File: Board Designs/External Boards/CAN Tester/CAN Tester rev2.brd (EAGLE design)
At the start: 83.8 x 100.3 mm, 27 parts, among them M1 Minifit, M2 Nanofit, M3 Nanofit-1, M4 Minifit-1, U1 ISOLATED CAN TRANSCIEVER, U3 TEENSY_3.2_SIMPLE, U4 CHARACTER_LCD

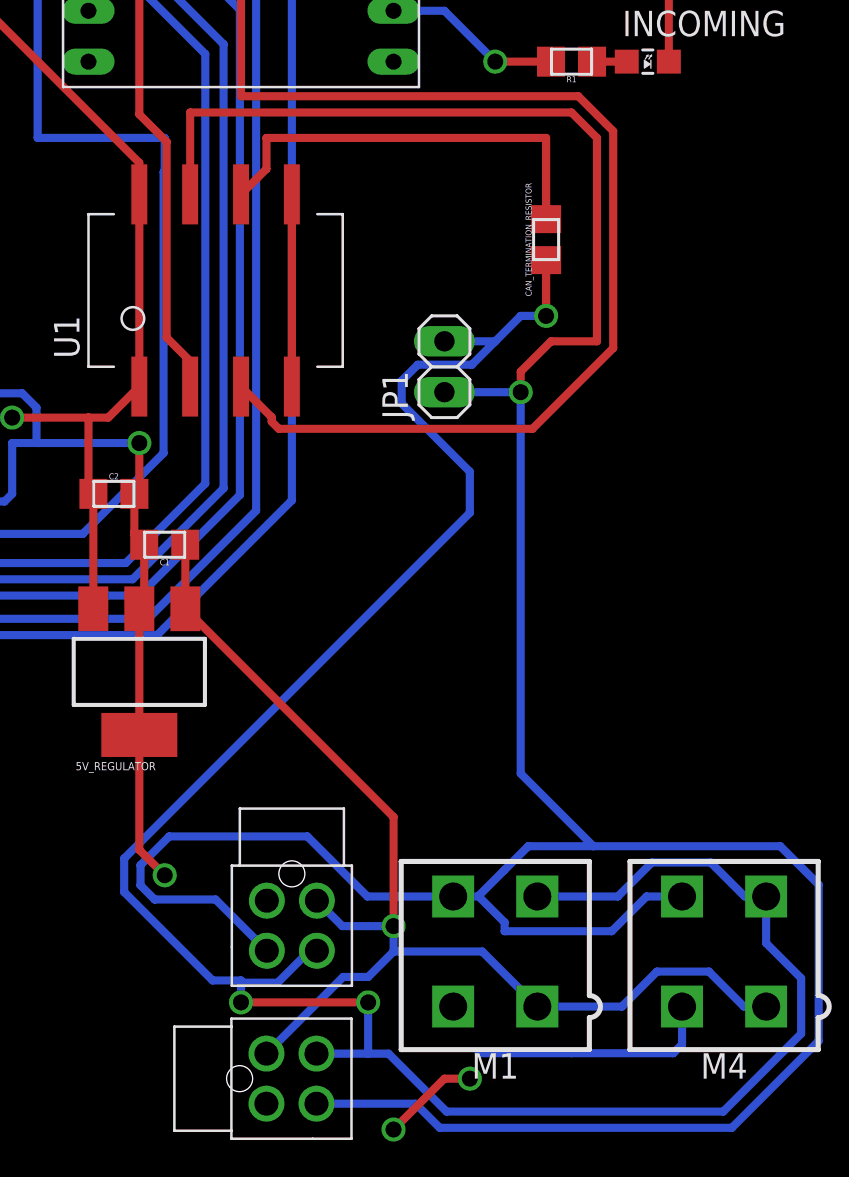
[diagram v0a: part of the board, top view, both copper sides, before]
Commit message: Began work on Rev 2 of CAN_Tester, fixing the existing issues with the Rev 1 board but not isolating the isocan yet.
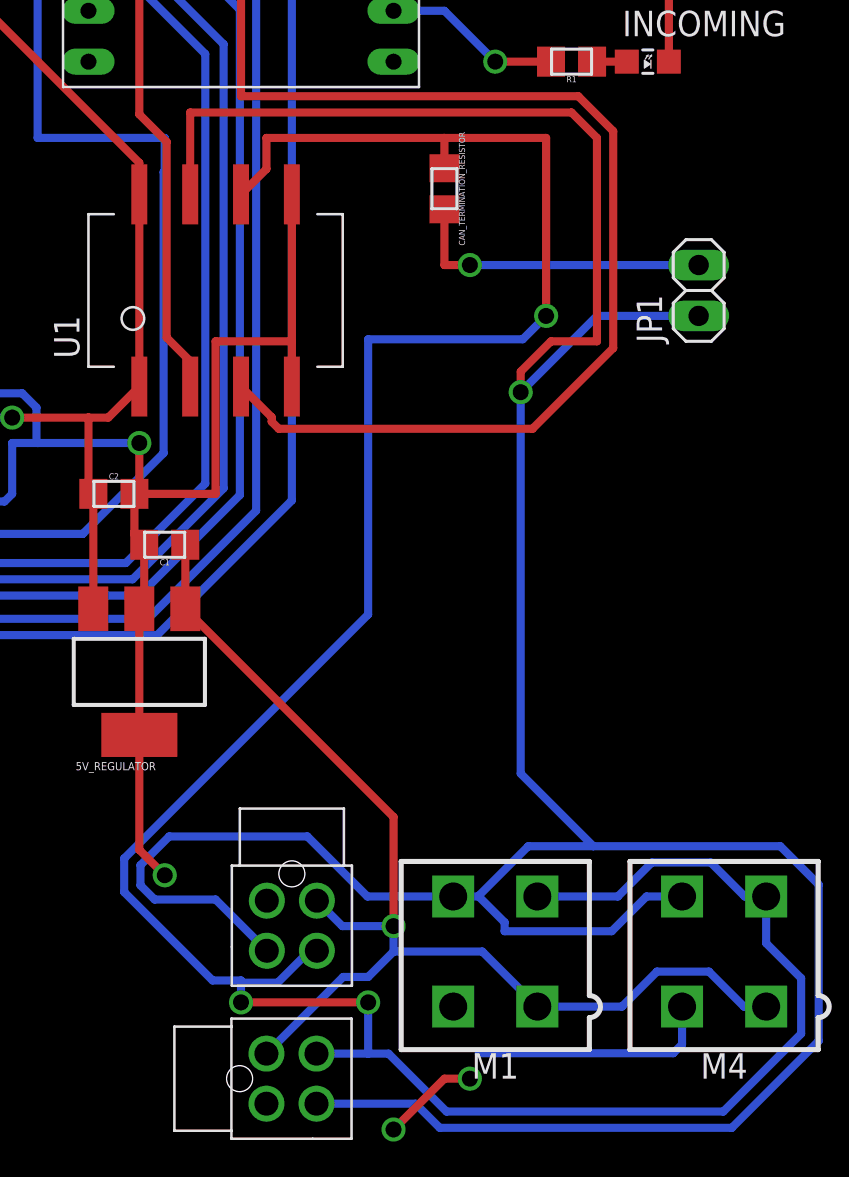
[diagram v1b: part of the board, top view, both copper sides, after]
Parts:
- moved JP1 13.3 mm to (74.9, 47.0)
- moved CAN_TERMINATION_RESISTOR 5.68 mm to (62.2, 52.1), turned to 270 degrees
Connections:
- removed net N$16: U1.P$4, U1.P$5
- new net N$15: CAN_TERMINATION_RESISTOR.2, JP1.2
- net CANL: no longer CAN_TERMINATION_RESISTOR.2, JP1.2
- net GND: now also U1.P$4, U1.P$5
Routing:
- net GND: track 213.6 -> 238.7 mm
- net N$15: track 0.00 -> 15.5 mm, vias 0 -> 1
- net N$16: track 9.60 -> 0.00 mm
- net CANH: track 161.8 -> 168.5 mm
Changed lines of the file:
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@@
 <?xml version="1.0" encoding="utf-8"?>
 <!DOCTYPE eagle SYSTEM "eagle.dtd">
-<eagle version="9.2.1">
+<eagle version="9.2.2">
 <drawing>
 <settings>
@@
 <attribute name="VALUE" x="45.72" y="36.1188" size="0.3048" layer="27" align="top-center"/>
 </element>
-<element name="CAN_TERMINATION_RESISTOR" library="HyTechDevices" package="0805" value="120" x="67.31" y="49.53" smashed="yes" rot="R90">
-<attribute name="NAME" x="66.5861" y="49.53" size="0.3048" layer="25" rot="R90" align="bottom-center"/>
-<attribute name="VALUE" x="68.0212" y="49.53" size="0.3048" layer="27" rot="R90" align="top-center"/>
+<element name="CAN_TERMINATION_RESISTOR" library="HyTechDevices" package="0805" value="120" x="62.23" y="52.07" smashed="yes" rot="R270">
+<attribute name="NAME" x="62.9539" y="52.07" size="0.3048" layer="25" rot="R270" align="bottom-center"/>
+<attribute name="VALUE" x="61.5188" y="52.07" size="0.3048" layer="27" rot="R270" align="top-center"/>
 </element>
 <element name="CONTRAST_POT" library="HyTechDevices" package="TRIM-3386" value="10k" x="33.02" y="88.9" smashed="yes" rot="R180">
@@
 <attribute name="VALUE" x="76.2" y="20.32" size="1.27" layer="27" align="bottom-center"/>
 </element>
-<element name="JP1" library="HyTechDevices" package="1X02" value="M02" x="62.23" y="43.18" smashed="yes" rot="R90">
-<attribute name="NAME" x="60.4012" y="40.5638" size="1.27" layer="25" ratio="10" rot="R90"/>
-<attribute name="VALUE" x="65.405" y="40.64" size="1.27" layer="27" rot="R90"/>
+<element name="JP1" library="HyTechDevices" package="1X02" value="M02" x="74.93" y="46.99" smashed="yes" rot="R90">
+<attribute name="NAME" x="73.1012" y="44.3738" size="1.27" layer="25" ratio="10" rot="R90"/>
+<attribute name="VALUE" x="78.105" y="44.45" size="1.27" layer="27" rot="R90"/>
 </element>
 </elements>
@@
 <contactref element="M1" pad="3"/>
 <contactref element="U1" pad="P$6"/>
-<contactref element="CAN_TERMINATION_RESISTOR" pad="1"/>
-<contactref element="CAN_TERMINATION_RESISTOR" pad="2"/>
 <contactref element="M3" pad="P$3"/>
 <contactref element="M4" pad="3"/>
 <wire x1="52.07" y1="51.79" x2="53.34" y2="53.06" width="0.4064" layer="1"/>
 <wire x1="53.34" y1="53.06" x2="53.34" y2="54.61" width="0.4064" layer="1"/>
-<wire x1="53.34" y1="54.61" x2="67.31" y2="54.61" width="0.4064" layer="1"/>
-<wire x1="67.31" y1="54.61" x2="67.31" y2="50.555" width="0.4064" layer="1"/>
 <wire x1="72.59211875" y1="18.4177" x2="75.53168125" y2="18.4177" width="0.4064" layer="16"/>
 <wire x1="66.87" y1="16.72" x2="70.89441875" y2="16.72" width="0.4064" layer="16"/>
@@
 <wire x1="80.0485" y1="12.63898125" x2="78.3" y2="14.38748125" width="0.4064" layer="16"/>
 <wire x1="78.3" y1="14.38748125" x2="78.3" y2="16.72" width="0.4064" layer="16"/>
-<wire x1="46.2344" y1="16.9409625" x2="46.2344" y2="18.6190375" width="0.4064" layer="16"/>
-<wire x1="63.5" y1="35.8846375" x2="46.2344" y2="18.6190375" width="0.4064" layer="16"/>
+<wire x1="46.2344" y1="18.6190375" x2="46.2344" y2="16.9409625" width="0.4064" layer="16"/>
 <wire x1="53.89858125" y1="12.4115" x2="52.07" y2="12.4115" width="0.4064" layer="16"/>
 <wire x1="52.07" y1="12.5258" x2="50.6495625" y2="12.5258" width="0.4064" layer="16"/>
@@
 <wire x1="58.42" y1="11.43" x2="58.42" y2="8.87" width="0.4064" layer="16"/>
 <wire x1="52.07" y1="12.4115" x2="52.07" y2="11.43" width="0.4064" layer="16"/>
-<contactref element="JP1" pad="2"/>
-<wire x1="67.31" y1="48.505" x2="67.31" y2="45.72" width="0.4064" layer="1"/>
 <via x="67.31" y="45.72" extent="1-16" drill="0.8" diameter="0.8"/>
-<wire x1="64.77" y1="44.45" x2="62.23" y2="44.45" width="0.4064" layer="16"/>
-<wire x1="67.31" y1="45.72" x2="66.04" y2="45.72" width="0.4064" layer="16"/>
-<wire x1="66.04" y1="45.72" x2="64.77" y2="44.45" width="0.4064" layer="16"/>
-<wire x1="60.8998625" y1="43.2816" x2="60.0964" y2="42.4781375" width="0.4064" layer="16"/>
-<wire x1="60.0964" y1="42.4781375" x2="60.0964" y2="41.3418625" width="0.4064" layer="16"/>
-<wire x1="60.0964" y1="41.3418625" x2="63.5" y2="37.9382625" width="0.4064" layer="16"/>
-<wire x1="63.5" y1="37.9382625" x2="63.5" y2="35.8846375" width="0.4064" layer="16"/>
-<wire x1="64.77" y1="44.45" x2="63.6016" y2="43.2816" width="0.4064" layer="16"/>
-<wire x1="63.6016" y1="43.2816" x2="60.8998625" y2="43.2816" width="0.4064" layer="16"/>
-<wire x1="67.31" y1="48.505" x2="67.31" y2="50.555" width="0" layer="19" extent="1-1"/>
+<wire x1="67.31" y1="54.61" x2="67.31" y2="45.72" width="0.4064" layer="1"/>
+<wire x1="53.34" y1="54.61" x2="62.23" y2="54.61" width="0.4064" layer="1"/>
+<wire x1="62.23" y1="54.61" x2="67.31" y2="54.61" width="0.4064" layer="1"/>
+<wire x1="67.31" y1="45.72" x2="66.1416" y2="44.5516" width="0.4064" layer="16"/>
+<wire x1="66.1416" y1="44.5516" x2="58.42" y2="44.5516" width="0.4064" layer="16"/>
+<wire x1="58.42" y1="44.5516" x2="58.42" y2="30.8046375" width="0.4064" layer="16"/>
+<wire x1="58.42" y1="30.8046375" x2="46.2344" y2="18.6190375" width="0.4064" layer="16"/>
+<contactref element="CAN_TERMINATION_RESISTOR" pad="1"/>
+<wire x1="62.23" y1="53.095" x2="62.23" y2="54.61" width="0.4064" layer="1"/>
 </signal>
 <signal name="GND">
@@
 <wire x1="66.80318125" y1="84.3534" x2="67.8266" y2="84.3534" width="0.4064" layer="1"/>
 <wire x1="67.8266" y1="84.3534" x2="73.44" y2="78.74" width="0.4064" layer="1"/>
-<wire x1="46.99" y1="24.79" x2="46.99" y2="24.13" width="0.4064" layer="1"/>
-<wire x1="46.99" y1="24.13" x2="46.99" y2="19.05" width="0.4064" layer="1"/>
+<wire x1="46.99" y1="24.79" x2="46.99" y2="19.05" width="0.4064" layer="1"/>
 <wire x1="46.99" y1="19.05" x2="48.26" y2="17.78" width="0.4064" layer="1"/>
 <via x="48.26" y="17.78" extent="1-16" drill="0.8" diameter="0.8"/>
-<wire x1="63.94" y1="8.89" x2="68.58" y2="8.89" width="0.4064" layer="16"/>
-<wire x1="68.58" y1="8.89" x2="73.66" y2="8.89" width="0.4064" layer="16"/>
+<wire x1="63.94" y1="8.89" x2="73.66" y2="8.89" width="0.4064" layer="16"/>
 <wire x1="73.66" y1="8.89" x2="74.1" y2="9.33" width="0.4064" layer="16"/>
 <wire x1="74.1" y1="9.33" x2="74.1" y2="11.22" width="0.4064" layer="16"/>
@@
 <wire x1="62.23" y1="7.62" x2="63.5" y2="7.62" width="0.4064" layer="1"/>
 <wire x1="46.99" y1="31.09" x2="46.99" y2="24.79" width="0.4064" layer="1"/>
-<wire x1="68.58" y1="8.89" x2="68.58" y2="8.89" width="0.4064" layer="16"/>
+<contactref element="U1" pad="P$5"/>
+<contactref element="U1" pad="P$4"/>
+<wire x1="54.61" y1="51.79" x2="54.61" y2="44.45" width="0.4064" layer="1"/>
+<wire x1="54.61" y1="44.45" x2="54.61" y2="42.19" width="0.4064" layer="1"/>
+<wire x1="46.745" y1="36.83" x2="50.8" y2="36.83" width="0.4064" layer="1"/>
+<wire x1="50.8" y1="36.83" x2="50.8" y2="44.45" width="0.4064" layer="1"/>
+<wire x1="50.8" y1="44.45" x2="54.61" y2="44.45" width="0.4064" layer="1"/>
 </signal>
 <signal name="CANH">
@@
 <via x="66.04" y="41.91" extent="1-16" drill="0.8" diameter="0.8"/>
 <wire x1="63.94381875" y1="16.72" x2="65.2358" y2="15.42801875" width="0.4064" layer="16"/>
-<contactref element="JP1" pad="1"/>
-<wire x1="62.23" y1="41.91" x2="66.04" y2="41.91" width="0.4064" layer="16"/>
 <wire x1="66.04" y1="41.91" x2="66.04" y2="42.935" width="0.4064" layer="1"/>
 <wire x1="66.04" y1="42.935" x2="67.555" y2="44.45" width="0.4064" layer="1"/>
 <wire x1="66.04" y1="41.91" x2="66.04" y2="22.86" width="0.4064" layer="16"/>
 <wire x1="66.04" y1="22.86" x2="69.6695" y2="19.2305" width="0.4064" layer="16"/>
-<wire x1="66.41839375" y1="19.2305" x2="65.2104" y2="18.02250625" width="0.4064" layer="16"/>
 <wire x1="69.6695" y1="19.2305" x2="66.41839375" y2="19.2305" width="0.4064" layer="16"/>
-<wire x1="65.2104" y1="18.02250625" x2="63.94381875" y2="16.755925" width="0.4064" layer="16"/>
+<wire x1="66.41839375" y1="19.2305" x2="63.94381875" y2="16.755925" width="0.4064" layer="16"/>
 <wire x1="63.94381875" y1="16.755925" x2="63.94381875" y2="16.72" width="0.4064" layer="16"/>
+<wire x1="69.85" y1="45.72" x2="66.04" y2="41.91" width="0.4064" layer="16"/>
+<contactref element="JP1" pad="1"/>
+<wire x1="74.93" y1="45.72" x2="69.85" y2="45.72" width="0.4064" layer="16"/>
 </signal>
 <signal name="CANRX">
@@
 <wire x1="65.0494" y1="90.4494" x2="67.8688" y2="90.4494" width="0.4064" layer="16"/>
 </signal>
-<signal name="N$16">
-<contactref element="U1" pad="P$5"/>
-<contactref element="U1" pad="P$4"/>
-<wire x1="54.61" y1="51.79" x2="54.61" y2="42.19" width="0.4064" layer="1"/>
-</signal>
 <signal name="VO">
 <contactref element="CONTRAST_POT" pad="2"/>
@@
 <wire x1="74.6506" y1="81.5594" x2="74.3712" y2="81.5594" width="0.4064" layer="16"/>
 </signal>
+<signal name="N$15">
+<contactref element="CAN_TERMINATION_RESISTOR" pad="2"/>
+<contactref element="JP1" pad="2"/>
+<wire x1="62.23" y1="51.045" x2="62.23" y2="48.26" width="0.4064" layer="1"/>
+<wire x1="62.23" y1="48.26" x2="63.5" y2="48.26" width="0.4064" layer="1"/>
+<via x="63.5" y="48.26" extent="1-16" drill="0.8" diameter="0.8"/>
+<wire x1="63.5" y1="48.26" x2="74.93" y2="48.26" width="0.4064" layer="16"/>
+</signal>
 </signals>
